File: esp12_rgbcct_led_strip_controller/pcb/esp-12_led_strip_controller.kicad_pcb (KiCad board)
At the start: 2 copper layers, 77 x 52 mm, 41 parts, among them J1 12V, J2 UART_M, J3 LED Strip, J4 UART_F, Q1 NPN_EBC, Q10 NMOSFET_GDS, Q2 NPN_EBC, Q3 NPN_EBC, Q4 NMOSFET_GDS, Q5 NMOSFET_GDS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

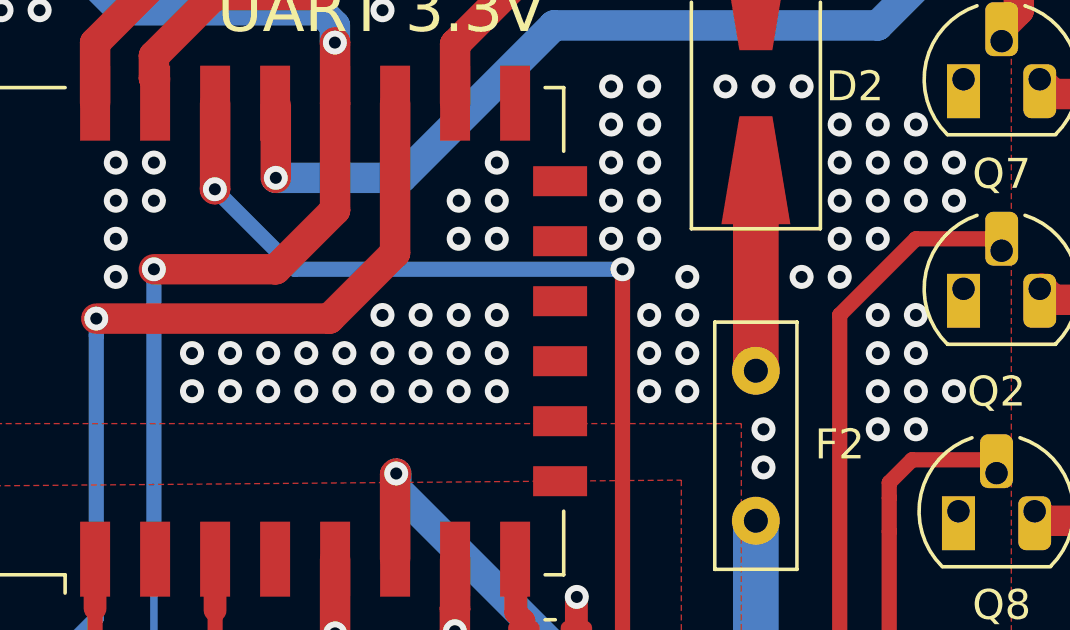
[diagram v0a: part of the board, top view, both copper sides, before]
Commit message: remove extra drill holes
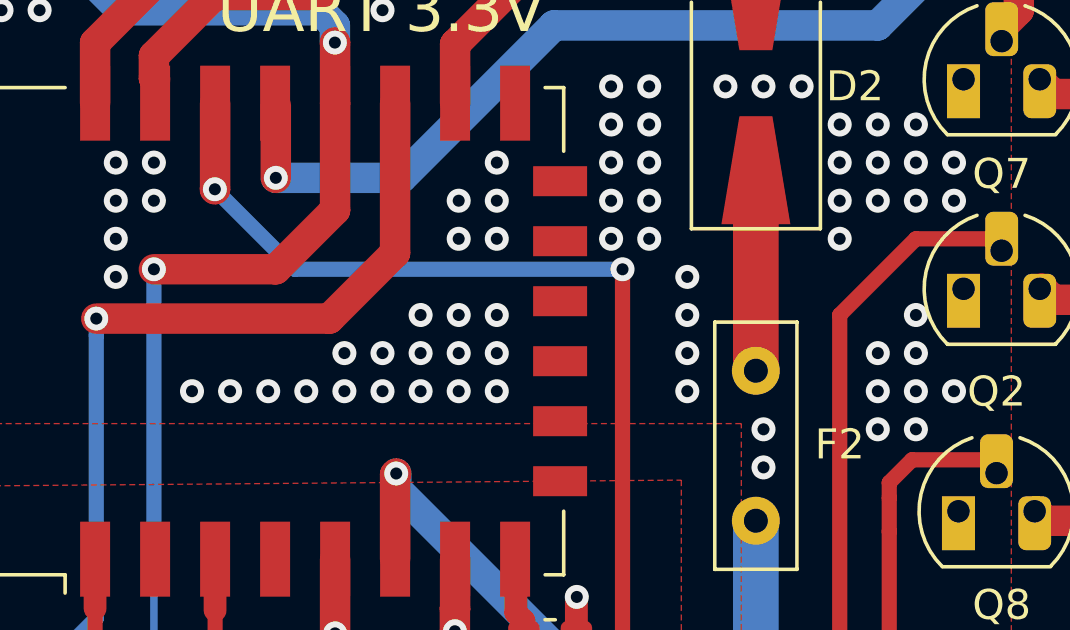
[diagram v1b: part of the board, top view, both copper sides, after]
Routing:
- net GND: vias 204 -> 192
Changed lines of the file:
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@@
     (thickness 1.6)
     (drawings 16)
-    (tracks 428)
+    (tracks 416)
     (zones 0)
     (modules 41)
@@
   (via (at 82.55 120.65) (size 0.8) (drill 0.4) (layers F.Cu B.Cu) (net 2))
   (via (at 83.82 119.38) (size 0.8) (drill 0.4) (layers F.Cu B.Cu) (net 2))
-  (via (at 82.55 119.38) (size 0.8) (drill 0.4) (layers F.Cu B.Cu) (net 2))
-  (via (at 80.01 118.11) (size 0.8) (drill 0.4) (layers F.Cu B.Cu) (net 2))
   (via (at 81.28 116.84) (size 0.8) (drill 0.4) (layers F.Cu B.Cu) (net 2))
-  (via (at 81.28 118.11) (size 0.8) (drill 0.4) (layers F.Cu B.Cu) (net 2))
-  (via (at 82.55 116.84) (size 0.8) (drill 0.4) (layers F.Cu B.Cu) (net 2))
   (via (at 82.55 115.57) (size 0.8) (drill 0.4) (layers F.Cu B.Cu) (net 2))
   (via (at 81.28 115.57) (size 0.8) (drill 0.4) (layers F.Cu B.Cu) (net 2))
@@
   (via (at 57.15 118.11) (size 0.8) (drill 0.4) (layers F.Cu B.Cu) (net 2))
   (via (at 59.69 121.92) (size 0.8) (drill 0.4) (layers F.Cu B.Cu) (net 2))
-  (via (at 59.69 120.65) (size 0.8) (drill 0.4) (layers F.Cu B.Cu) (net 2))
-  (via (at 60.96 120.65) (size 0.8) (drill 0.4) (layers F.Cu B.Cu) (net 2))
   (via (at 60.96 121.92) (size 0.8) (drill 0.4) (layers F.Cu B.Cu) (net 2))
   (via (at 62.23 121.92) (size 0.8) (drill 0.4) (layers F.Cu B.Cu) (net 2))
-  (via (at 62.23 120.65) (size 0.8) (drill 0.4) (layers F.Cu B.Cu) (net 2))
-  (via (at 63.5 120.65) (size 0.8) (drill 0.4) (layers F.Cu B.Cu) (net 2))
   (via (at 63.5 121.92) (size 0.8) (drill 0.4) (layers F.Cu B.Cu) (net 2))
   (via (at 64.77 121.92) (size 0.8) (drill 0.4) (layers F.Cu B.Cu) (net 2))
   (via (at 64.77 120.65) (size 0.8) (drill 0.4) (layers F.Cu B.Cu) (net 2))
   (via (at 66.04 120.65) (size 0.8) (drill 0.4) (layers F.Cu B.Cu) (net 2))
-  (via (at 66.04 119.38) (size 0.8) (drill 0.4) (layers F.Cu B.Cu) (net 2))
   (via (at 67.31 119.38) (size 0.8) (drill 0.4) (layers F.Cu B.Cu) (net 2))
   (via (at 68.58 119.38) (size 0.8) (drill 0.4) (layers F.Cu B.Cu) (net 2))
@@
   (via (at 73.66 116.84) (size 0.8) (drill 0.4) (layers F.Cu B.Cu) (net 2))
   (via (at 76.2 118.11) (size 0.8) (drill 0.4) (layers F.Cu B.Cu) (net 2))
-  (via (at 74.93 119.38) (size 0.8) (drill 0.4) (layers F.Cu B.Cu) (net 2))
   (via (at 76.2 119.38) (size 0.8) (drill 0.4) (layers F.Cu B.Cu) (net 2))
   (via (at 76.2 120.65) (size 0.8) (drill 0.4) (layers F.Cu B.Cu) (net 2))
-  (via (at 74.93 120.65) (size 0.8) (drill 0.4) (layers F.Cu B.Cu) (net 2))
-  (via (at 74.93 121.92) (size 0.8) (drill 0.4) (layers F.Cu B.Cu) (net 2))
   (via (at 76.2 121.92) (size 0.8) (drill 0.4) (layers F.Cu B.Cu) (net 2))
   (via (at 78.74 123.19) (size 0.8) (drill 0.4) (layers F.Cu B.Cu) (net 2))
